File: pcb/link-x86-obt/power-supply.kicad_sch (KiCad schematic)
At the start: 11 parts, among them J2 DF63-5P-3.96DSA

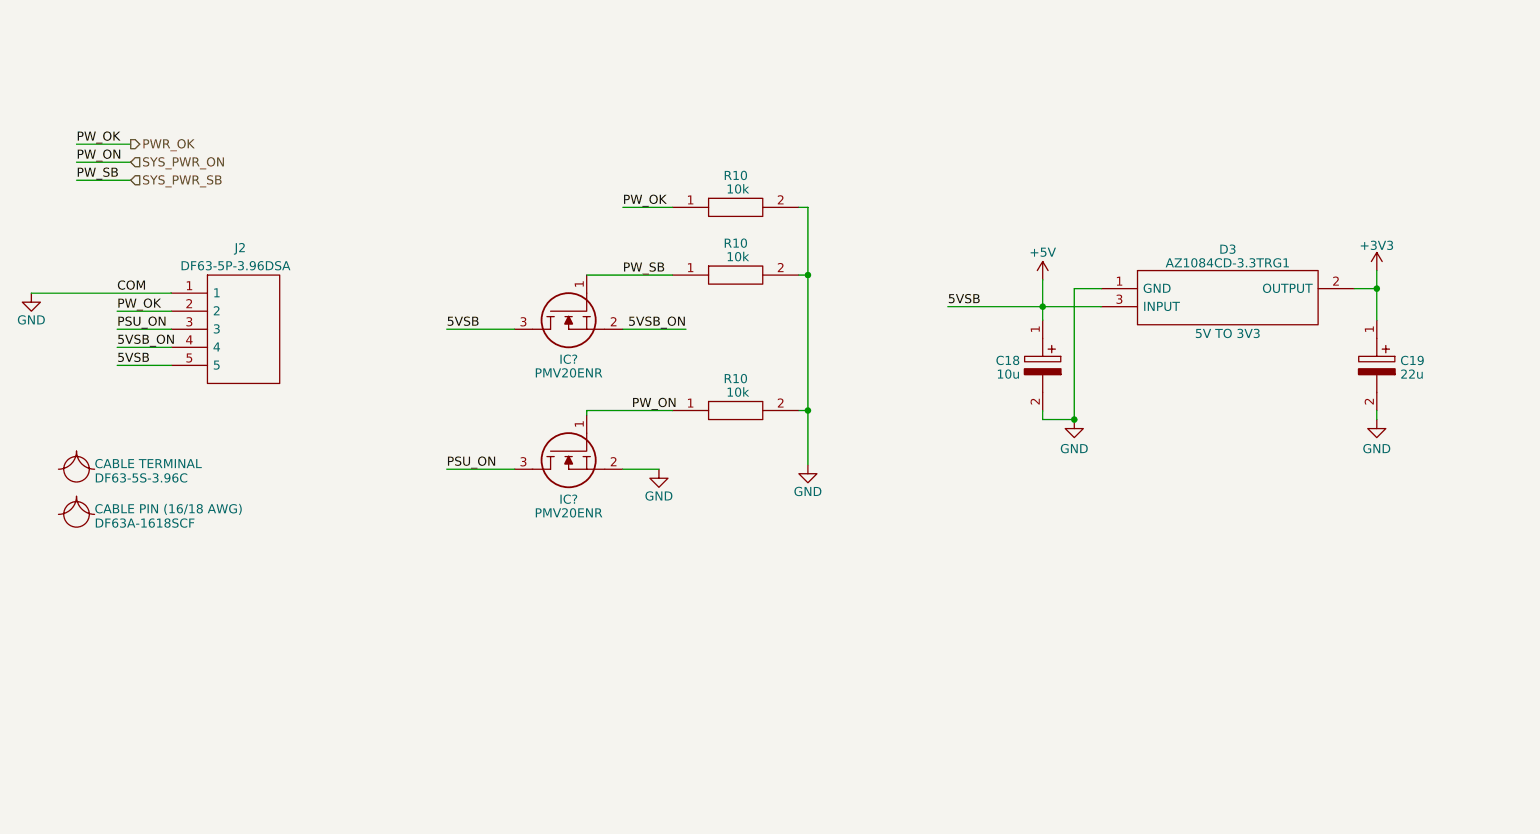
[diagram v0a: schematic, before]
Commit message: add P-channel mosfet to 5VSB line
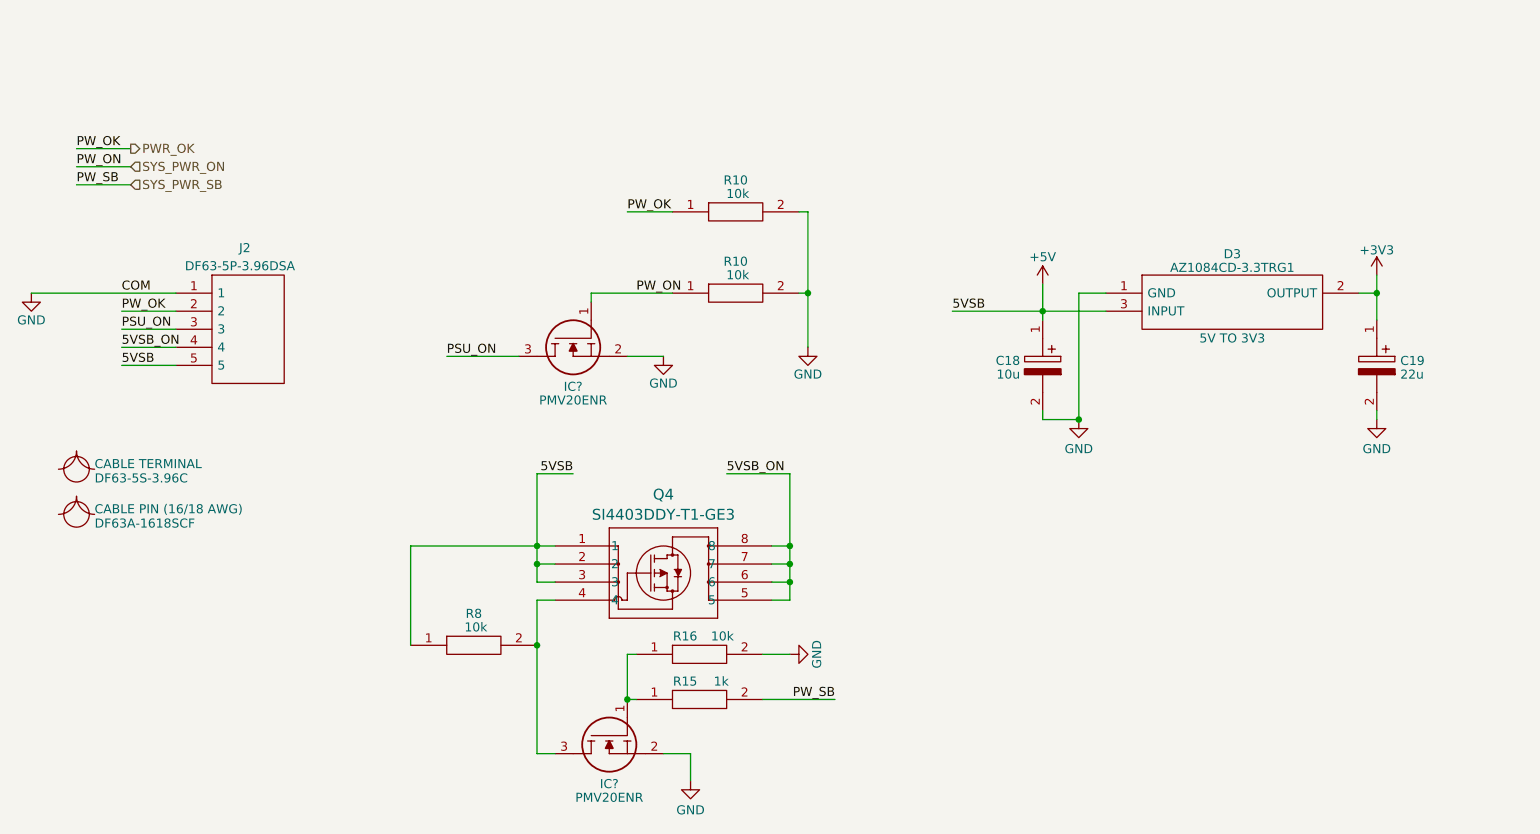
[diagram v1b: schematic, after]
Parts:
- removed R10: 10k, RESC1005X40N, symbol SamacSys_Parts:RK73H1ETTP1002F
- added Q4: SI4403DDY-T1-GE3, Oro:SO-8_MS-012_VIS, symbol Oro:SI4403DDY-T1-GE3
- added R15: 1k, RESC2012X60N, symbol SamacSys_Parts:SG73P2ATTD102J
- added R16, R8: 10k, RESC1005X40N, symbol SamacSys_Parts:RK73H1ETTP1002F
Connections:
- net +5V: now also Q4.1, Q4.2, Q4.3, R8.1; no longer IC?.3
- net 5VSB_ON: now also Q4.5, Q4.6, Q4.7, Q4.8; no longer IC?.2
- net GND: now also IC?.2, R16.2
- net SYS_PWR_SB: now also R15.2; no longer IC?.1
- new net: IC?.1, R15.1, R16.1
- new net: IC?.3, Q4.4, R8.2
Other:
- moved on the sheet: D3, IC?, J2, R10

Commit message: omit ethernet enable mosfets in lieu of reset mosfet
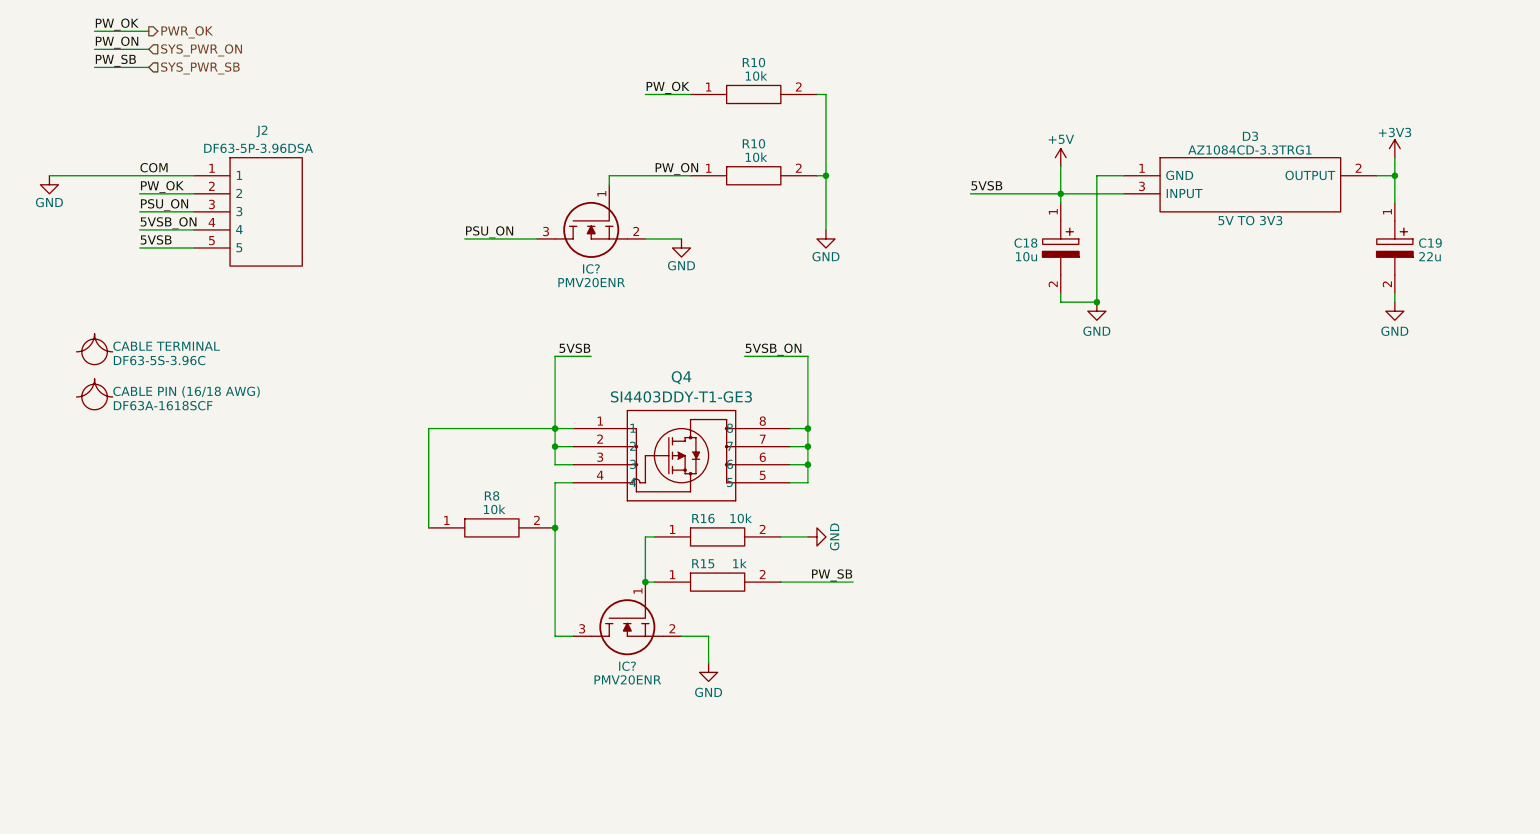
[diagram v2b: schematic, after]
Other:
- moved on the sheet: C18, C19, D3, IC?, J2, Q4, R10, R15, R16, R8

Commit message: initial test of new board
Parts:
- added TP3: 5V, TestPoint:TestPoint_Pad_D1.0mm, symbol Connector:TestPoint
- added TP4: 5V PW_ON, TestPoint:TestPoint_Pad_D1.0mm, symbol Connector:TestPoint
- added TP5: 3V3, TestPoint:TestPoint_Pad_D1.0mm, symbol Connector:TestPoint
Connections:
- net +3V3: now also TP5.1
- net +5V: now also TP3.1
- net 5VSB_ON: now also TP4.1
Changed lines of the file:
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@@
 	)
 	(junction
+		(at 251.46 78.74)
+		(diameter 0)
+		(color 0 0 0 0)
+	)
+	(junction
 		(at 156.21 119.38)
 		(diameter 0)
@@
 	)
 	(junction
+		(at 102.87 114.3)
+		(diameter 0)
+		(color 0 0 0 0)
+	)
+	(junction
 		(at 133.35 135.89)
 		(diameter 0)
@@
 	(wire
 		(pts
+			(xy 251.46 78.74) (xy 238.76 78.74)
+		)
+		(stroke
+			(width 0)
+			(type default)
+		)
+	)
+	(wire
+		(pts
 			(xy 238.76 76.2) (xy 238.76 78.74)
 		)
@@
 	(wire
 		(pts
+			(xy 251.46 82.55) (xy 251.46 78.74)
+		)
+		(stroke
+			(width 0)
+			(type default)
+		)
+	)
+	(wire
+		(pts
 			(xy 120.65 121.92) (xy 123.19 121.92)
 		)
@@
 	(wire
 		(pts
+			(xy 156.21 114.3) (xy 160.02 114.3)
+		)
+		(stroke
+			(width 0)
+			(type default)
+		)
+	)
+	(wire
+		(pts
 			(xy 120.65 143.51) (xy 123.19 143.51)
 		)
@@
 		(length 2.54)
 		(shape round)
-		(at 238.76 78.74 270)
+		(at 251.46 82.55 270)
 		(effects
 			(font
@@
 		)
 		(property "Netclass" "3V3"
-			(at 245.745 78.74 0)
+			(at 258.445 82.55 0)
 			(effects
 				(font
@@
 	)
 	(symbol
+		(lib_id "Connector:TestPoint")
+		(at 160.02 114.3 0)
+		(unit 1)
+		(exclude_from_sim no)
+		(in_bom yes)
+		(on_board yes)
+		(dnp no)
+		(property "Reference" "TP4"
+			(at 161.417 109.7858 0)
+			(effects
+				(font
+					(size 1.27 1.27)
+				)
+				(justify left)
+			)
+		)
+		(property "Value" "5V PW_ON"
+			(at 161.417 112.2101 0)
+			(effects
+				(font
+					(size 1.27 1.27)
+				)
+				(justify left)
+			)
+		)
+		(property "Footprint" "TestPoint:TestPoint_Pad_D1.0mm"
+			(at 165.1 114.3 0)
+			(effects
+				(font
+					(size 1.27 1.27)
+				)
+				(hide yes)
+			)
+		)
+		(property "Datasheet" "~"
+			(at 165.1 114.3 0)
+			(effects
+				(font
+					(size 1.27 1.27)
+				)
+				(hide yes)
+			)
+		)
+		(property "Description" "test point"
+			(at 160.02 114.3 0)
+			(effects
+				(font
+					(size 1.27 1.27)
+				)
+				(hide yes)
+			)
+		)
+		(pin "1"
+		)
+		(instances
+			(project "OroLink"
+				(path "/e89dcd22-1250-4a5b-b778-1c95a0dd623d/f955395e-bf1a-4ef3-9cfe-ec9d49f66988"
+					(reference "TP4")
+					(unit 1)
+				)
+			)
+		)
+	)
+	(symbol
 		(lib_id "power:+3V3")
 		(at 238.76 76.2 0)
@@
 	)
 	(symbol
+		(lib_id "Connector:TestPoint")
+		(at 251.46 78.74 0)
+		(unit 1)
+		(exclude_from_sim no)
+		(in_bom yes)
+		(on_board yes)
+		(dnp no)
+		(property "Reference" "TP5"
+			(at 252.857 74.2258 0)
+			(effects
+				(font
+					(size 1.27 1.27)
+				)
+				(justify left)
+			)
+		)
+		(property "Value" "3V3"
+			(at 252.857 76.6501 0)
+			(effects
+				(font
+					(size 1.27 1.27)
+				)
+				(justify left)
+			)
+		)
+		(property "Footprint" "TestPoint:TestPoint_Pad_D1.0mm"
+			(at 256.54 78.74 0)
+			(effects
+				(font
+					(size 1.27 1.27)
+				)
+				(hide yes)
+			)
+		)
+		(property "Datasheet" "~"
+			(at 256.54 78.74 0)
+			(effects
+				(font
+					(size 1.27 1.27)
+				)
+				(hide yes)
+			)
+		)
+		(property "Description" "test point"
+			(at 251.46 78.74 0)
+			(effects
+				(font
+					(size 1.27 1.27)
+				)
+				(hide yes)
+			)
+		)
+		(pin "1"
+		)
+		(instances
+			(project "OroLink"
+				(path "/e89dcd22-1250-4a5b-b778-1c95a0dd623d/f955395e-bf1a-4ef3-9cfe-ec9d49f66988"
+					(reference "TP5")
+					(unit 1)
+				)
+			)
+		)
+	)
+	(symbol
 		(lib_id "power:GND")
 		(at 138.43 87.63 0)
@@
 					(unit 1)
 				)
+			)
+		)
+	)
+	(symbol
+		(lib_id "Connector:TestPoint")
+		(at 102.87 114.3 0)
+		(unit 1)
+		(exclude_from_sim no)
+		(in_bom yes)
+		(on_board yes)
+		(dnp no)
+		(property "Reference" "TP3"
+			(at 104.267 109.7858 0)
+			(effects
+				(font
+					(size 1.27 1.27)
+				)
+				(justify left)
+			)
+		)
+		(property "Value" "5V"
+			(at 104.267 112.2101 0)
+			(effects
+				(font
+					(size 1.27 1.27)
+				)
+				(justify left)
+			)
+		)
+		(property "Footprint" "TestPoint:TestPoint_Pad_D1.0mm"
+			(at 107.95 114.3 0)
+			(effects
+				(font
+					(size 1.27 1.27)
+				)
+				(hide yes)
+			)
+		)
+		(property "Datasheet" "~"
+			(at 107.95 114.3 0)
+			(effects
+				(font
+					(size 1.27 1.27)
+				)
+				(hide yes)
+			)
+		)
+		(property "Description" "test point"
+			(at 102.87 114.3 0)
+			(effects
+				(font
+					(size 1.27 1.27)
+				)
+				(hide yes)
+			)
+		)
+		(pin "1"
+		)
+		(instances
+			(project "OroLink"
+				(path "/e89dcd22-1250-4a5b-b778-1c95a0dd623d/f955395e-bf1a-4ef3-9cfe-ec9d49f66988"
+					(reference "TP3")
+					(unit 1)
+				)
